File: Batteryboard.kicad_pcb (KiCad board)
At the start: 4 copper layers, 76.2 x 76.2 mm, 147 parts, among them IC1 FAN4010IL6X_F113, IC2 FAN4010IL6X_F113, IC3 FAN4010IL6X_F113, J1 Conn_01x02_Male, J2 Conn_01x03_Male, J3 Conn_01x05_Male, J4 Conn_01x02_Male, J5 SC_19-20, Q1 SI7617DN-T1-GE3, Q2 SI7617DN-T1-GE3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

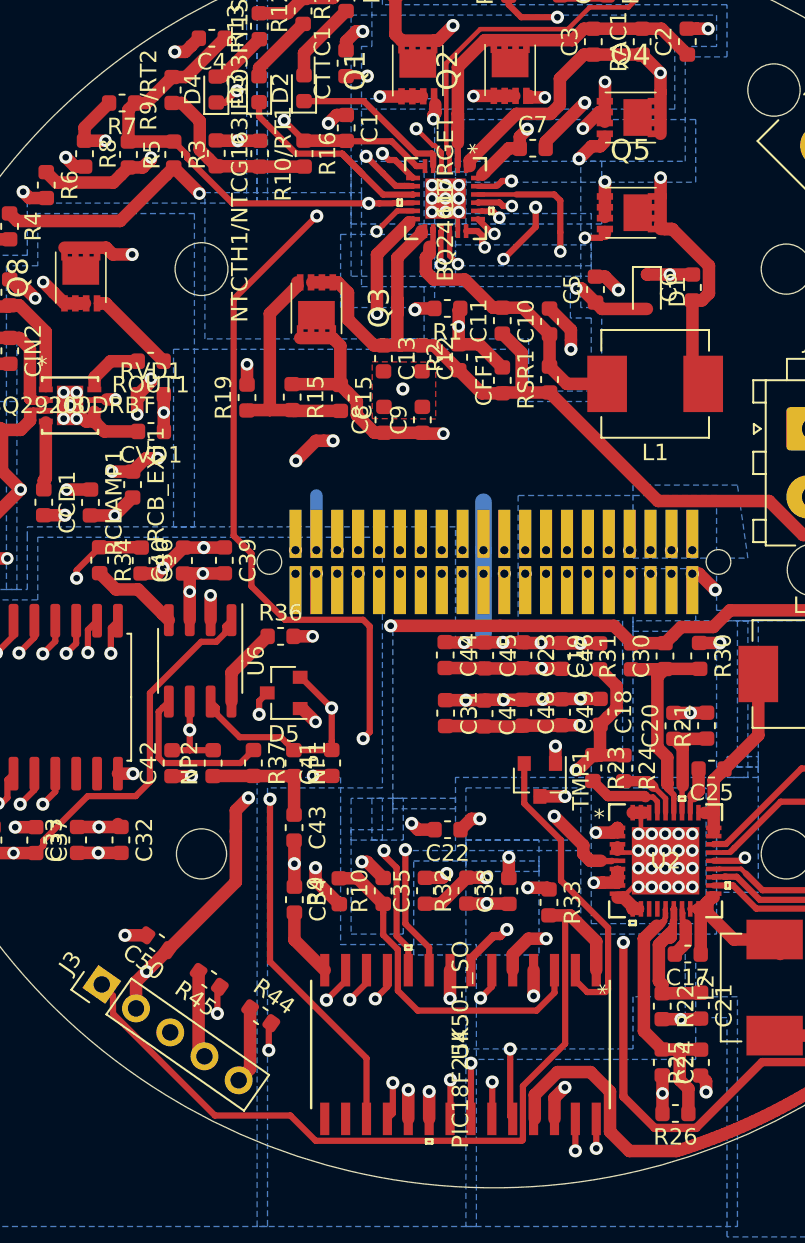
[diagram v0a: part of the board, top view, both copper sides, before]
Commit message: fixed some stuff, grounding and a few traces
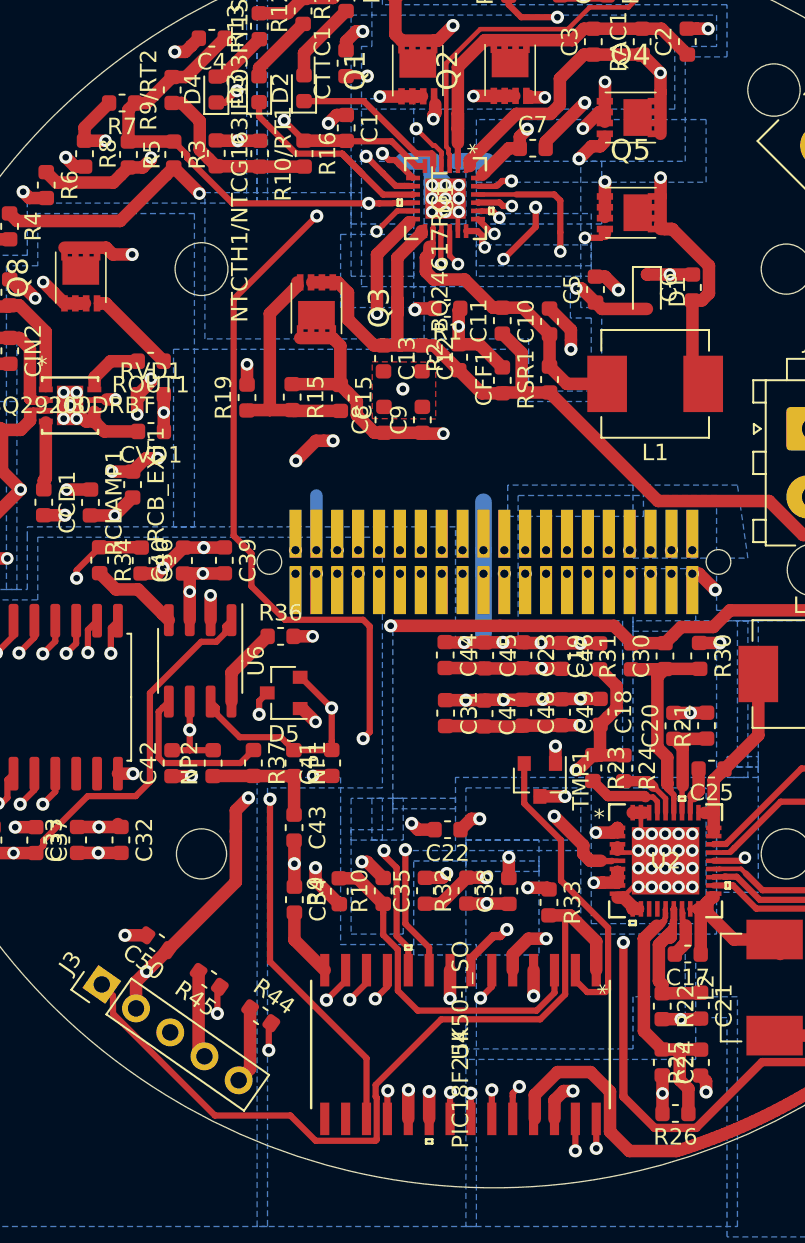
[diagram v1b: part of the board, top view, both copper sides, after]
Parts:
- added R_JUMP1: 0Ohm, Resistor_SMD:R_0603_1608Metric, B.Cu at (232.4, 38.7)
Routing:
- net PGND2: track 147.4 -> 156.1 mm
- net VBATCURRENT: track 44.3 -> 35.7 mm
- net 3V3: track 129.3 -> 134.2 mm
- net SI: track 58.8 -> 54.4 mm
- net SCK: track 61.6 -> 58.5 mm
- net MCLR: track 50.3 -> 48.7 mm
- net INT: track 61.2 -> 60.0 mm
- net PGC: track 26.1 -> 25.2 mm
- net CS: track 62.4 -> 61.6 mm

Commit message: fixed another little trace
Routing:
- net TS: track 85.7 -> 90.1 mm
- net MCLR: track 48.7 -> 49.3 mm

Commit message: big overhaul on board, did a bunch of stuff
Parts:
- C20, C21, C34, C35, C38, C50: value C -> .1uF
- C26, C27: value C -> 50nF
- J5: footprint MASA-LIB:bottom_Stack_Connector_2019_2020 -> MASA-LIB:Stack_Connector_2019_2020
- R10, R32, R9: value R_US -> 10kOhm
- R21, R22: value R_US -> 60.4kOhm
- R28: value R_US -> 30Ohm
- R33: value R_US -> 470Ohm
- R44, R45: value R_US -> 100Ohm
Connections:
- C1 pad 1: PGND2 -> VSS
- C10 pad 2: PGND2 -> VSS
- C2 pad 2: PGND2 -> VSS
- C20 pad 2: PGND2 -> VSS
- C21 pad 2: PGND2 -> VSS
- C26 pad 1: PGND2 -> VSS
- C27 pad 1: PGND2 -> VSS
- C28 pad 1: PGND2 -> VSS
- C29 pad 1: PGND2 -> VSS
- C32 pad 2: PGND2 -> VSS
- C33 pad 1: PGND2 -> VSS
- C34 pad 1: PGND2 -> VSS
- C35 pad 2: PGND2 -> VSS
- C36 pad 2: PGND2 -> VSS
- C37 pad 1: PGND2 -> VSS
- C38 pad 2: PGND2 -> VSS
- C39 pad 1: PGND2 -> VSS
- C4 pad 2: PGND2 -> VSS
- C40 pad 2: PGND2 -> VSS
- C41 pad 1: PGND2 -> VSS
- C42 pad 1: PGND2 -> VSS
- C43 pad 2: PGND2 -> VSS
- C50 pad 2: PGND2 -> VSS
- C7 pad 2: PGND2 -> VSS
- CTTC1 pad 2: PGND2 -> VSS
- D5 pad 1: PGND2 -> VSS
- IC1 pad 5: PGND2 -> VSS
- IC2 pad 5: PGND2 -> VSS
- IC3 pad 5: PGND2 -> VSS
- J3 pad 3: PGND2 -> VSS
- J5 pad 1: PGND2 -> VSS
- J5 pad 19: PGND2 -> VSS
- J5 pad 20: PGND2 -> VSS
- J5 pad 36: PGND2 -> VSS
- J5 pad 37: PGND2 -> VSS
- J5 pad 4: PGND2 -> VSS
- J5 pad 40: PGND2 -> VSS
- J5 pad 5: PGND2 -> VSS
- NTCTH1/NTCG163JF103FT1S1 pad 1: PGND2 -> VSS
- R1 pad 2: PGND2 -> VSS
- R10/RT1 pad 1: PGND2 -> VSS
- R21 pad 2: PGND2 -> VSS
- R22 pad 2: PGND2 -> VSS
- R25 pad 1: PGND2 -> VSS
- R28 pad 1: PGND2 -> VSS
- R30 pad 1: PGND2 -> VSS
- R36 pad 2: PGND2 -> VSS
- R38 pad 1: PGND2 -> VSS
- R4 pad 2: PGND2 -> VSS
- R41 pad 2: PGND2 -> VSS
- R42 pad 2: PGND2 -> VSS
- R6 pad 2: PGND2 -> VSS
- R8 pad 2: PGND2 -> VSS
- R_JUMP1 pad 1: PGND2 -> VSS
- TMP1 pad 3: PGND2 -> VSS
- U1 pad 25: PGND2 -> VSS
- U2 pad 23: PGND2 -> VSS
- U2 pad 3: PGND2 -> VSS
- U2 pad 4: PGND2 -> VSS
- U4 pad 19: PGND2 -> VSS
- U4 pad 8: PGND2 -> VSS
- U5 pad 18: PGND2 -> VSS
- U6 pad 2: PGND2 -> VSS
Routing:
- net VSS: track 0.00 -> 113.3 mm, vias 0 -> 47
- net PGND2: track 156.1 -> 57.7 mm, vias 94 -> 44
- net V7V: track 12.4 -> 14.3 mm
- net Net-(R19-Pad2): track 27.8 -> 28.9 mm
- net CAN_L: vias 3 -> 2
- net CAN_H: vias 2 -> 1
- net 5V0: vias 15 -> 11
- net 3V3: vias 8 -> 4
- added copper zone on B.Cu, net (none)
- added copper zone on B.Cu, net VSS

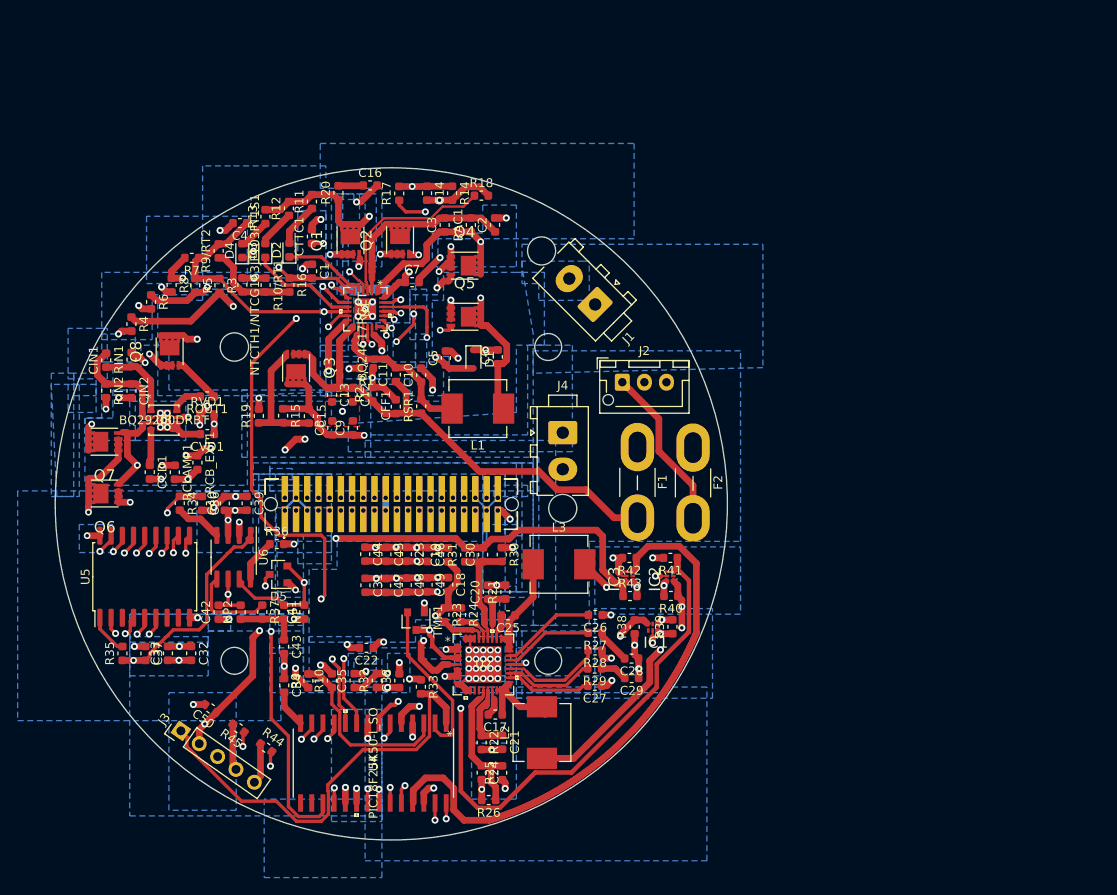
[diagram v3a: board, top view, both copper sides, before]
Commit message: basically an emergency backup, going to reroute my board
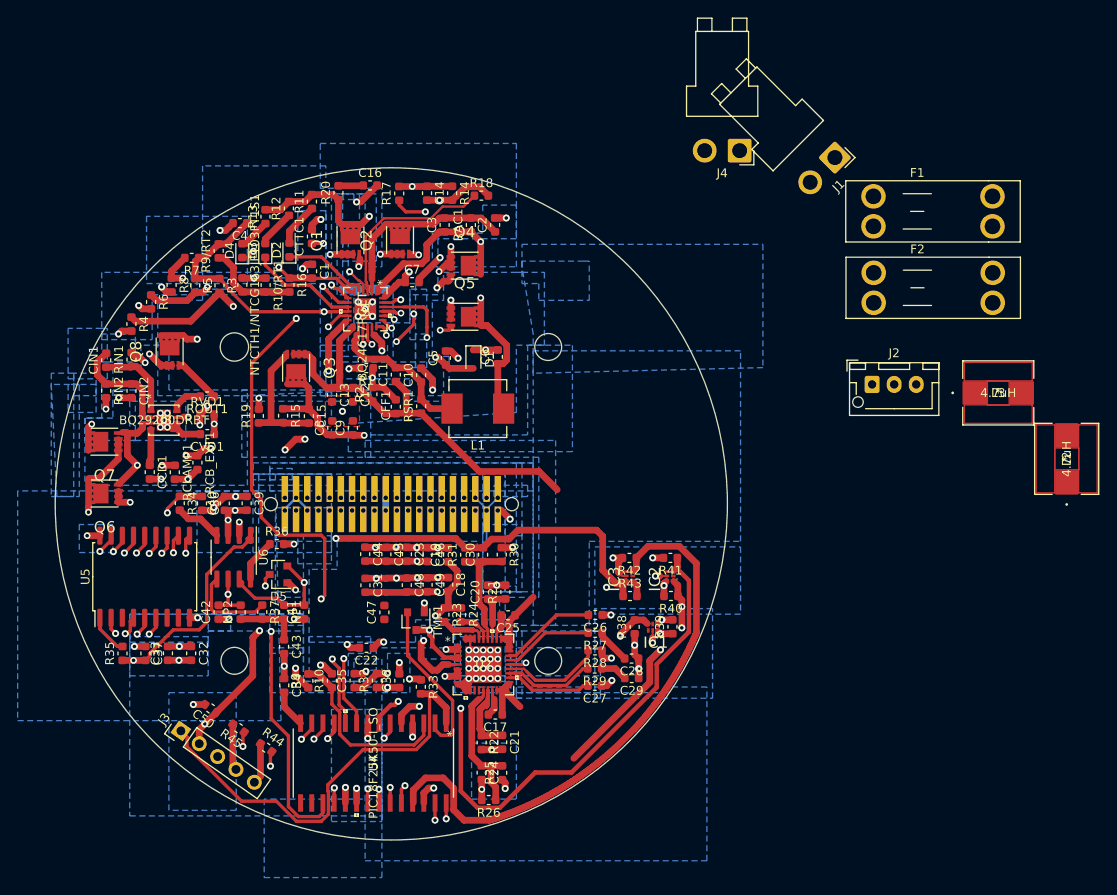
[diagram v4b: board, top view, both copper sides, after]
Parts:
- C20, C21: value .1uF -> 1nF
- C24, C30: value C -> 1nF
- C28, C29: value C -> .012uF
- C47: value 22uF -> 33uF
- F1, F2: footprint Fuse:Fuse_Blade_Mini_directSolder -> 3557-2:Fuseholder_Blade_Mini_Keystone_3557-2
- J1, J4: footprint Connector_TE-Connectivity:TE_MATE-N-LOK_1-770866-x_1x02_P4.14mm_Vertical -> Connector_JST:JST_VH_B2PS-VH_1x02_P3.96mm_Horizontal
- J5: footprint MASA-LIB:Stack_Connector_2019_2020 -> MASA-LIB:bottom_Stack_Connector_2019_2020
- L2, L3: footprint Inductor_SMD:L_Vishay_IHLP-2525 -> SRP7030-4R7M:SRP7030-4R7M
- R25: value R_US -> 5.36kOhm
- R26, R31: value R_US -> 40.2kOhm
- R27: value R_US -> 14kOhm
- R28: value 30Ohm -> 31Ohm
- R29: value R_US -> 9.31kOhm
- R30: value R_US -> 8.87kOhm
- R38, R41, R42: value R_US -> 5kOhm
- moved L2 67.1 mm to (311.9, 58.0)
- moved L3 53.4 mm to (304.2, 50.5)
- moved F1 39.0 mm to (290.0, 28.2), turned to 0 degrees
- moved J4 37.7 mm to (274.9, 23.0), turned to 180 degrees
- moved J1 31.9 mm to (285.6, 23.8)
- moved F2 28.5 mm to (290.0, 36.9), turned to 0 degrees
- moved J2 28.3 mm to (289.9, 49.5)
- moved C47 3.05 mm to (234.6, 75.4), turned to 90 degrees
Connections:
- C44 pad 2: Net-(C23-Pad2) -> Net-(C44-Pad2)
- C47 pad 1: PGND2 -> Net-(C47-Pad1)
- C47 pad 2: Net-(C31-Pad2) -> PGND2
- C8 pad 1: Q4D -> SRN
- C9 pad 1: Q4D -> SRN
- IC1 pad 1: Q4D -> SRN
- IC2 pad 1: Net-(C23-Pad2) -> Net-(C44-Pad2)
- IC3 pad 1: Net-(C31-Pad2) -> Net-(C47-Pad1)
- L2 pad 1: Net-(C23-Pad2) -> Net-(C44-Pad2)
- L3 pad 2: Net-(C31-Pad2) -> Net-(C47-Pad1)
- R39 pad 2: Q4D -> SRN
- R40 pad 1: Net-(C23-Pad2) -> Net-(C44-Pad2)
- R43 pad 2: Net-(C31-Pad2) -> Net-(C47-Pad1)
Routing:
- net Q6S: track 107.9 -> 71.1 mm
- net Net-(F2-Pad1): track 70.3 -> 50.5 mm
- net Net-(J2-Pad2): track 70.6 -> 51.8 mm
- net Net-(J1-Pad1): track 50.8 -> 35.5 mm
- net Net-(C31-Pad2): track 38.9 -> 27.7 mm, vias 3 -> 2
- net SRN: track 60.3 -> 49.9 mm
- net Net-(F1-Pad1): track 9.50 -> 0.00 mm
- net Net-(C23-Pad2): track 71.2 -> 67.1 mm
- net Net-(C47-Pad1): track 0.00 -> 3.73 mm
- net Net-(C25-Pad1): track 12.2 -> 8.51 mm
- net LX1: track 10.4 -> 7.41 mm
- net PGND2: track 57.7 -> 59.2 mm

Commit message: here u go matt, thanks for helping make this bomb
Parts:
- moved L2 65.5 mm to (254.1, 88.7)
- moved L3 52.6 mm to (255.3, 69.8), turned to 90 degrees
- moved RCB_EXT1 14.1 mm to (201.1, 51.5)
- moved R9 12.0 mm to (238.0, 83.7), turned to 270 degrees
- moved RVD1 8.15 mm to (208.2, 47.8), turned to 270 degrees
- moved R10 6.93 mm to (235.6, 83.7)
- moved R33 5.69 mm to (233.0, 83.6)
- moved C38 5.67 mm to (230.7, 83.7)
- moved R32 5.67 mm to (228.1, 83.6)
- moved C35 5.67 mm to (225.6, 83.6)
- moved CCD1 2.76 mm to (210.7, 59.0)
- moved RCLAMP1 2.39 mm to (208.5, 59.0), turned to 90 degrees
- moved Q8 2.09 mm to (212.3, 45.9)
- moved CVD1 1.90 mm to (214.5, 53.3), turned to 0 degrees
- moved C26 1.70 mm to (260.2, 75.7)
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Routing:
- net 3V3: track 134.2 -> 6.38 mm, vias 4 -> 0
- net Q4D: track 125.0 -> 5.58 mm, vias 3 -> 0
- net TS: track 90.1 -> 0.00 mm, vias 4 -> 0
- net VSS: track 113.3 -> 25.5 mm, vias 47 -> 7
- net Q6S: track 71.1 -> 1.14 mm, vias 4 -> 0
- net 5VCURRENT: track 67.2 -> 0.00 mm, vias 2 -> 0
- net 3V3CURRENT: track 65.2 -> 0.00 mm
- net Net-(C23-Pad2): track 67.1 -> 4.69 mm, vias 4 -> 0
- net CS: track 61.6 -> 0.00 mm, vias 2 -> 0
- net VBAT: track 69.1 -> 7.95 mm, vias 5 -> 0
- net INT: track 60.0 -> 0.00 mm, vias 2 -> 0
- net SO: track 59.9 -> 0.00 mm, vias 2 -> 0
- net SCK: track 58.5 -> 0.00 mm, vias 2 -> 0
- net SI: track 54.4 -> 0.00 mm, vias 2 -> 0
- net RESET: track 52.4 -> 0.00 mm, vias 2 -> 0
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- removed copper zone on B.Cu, net (none)

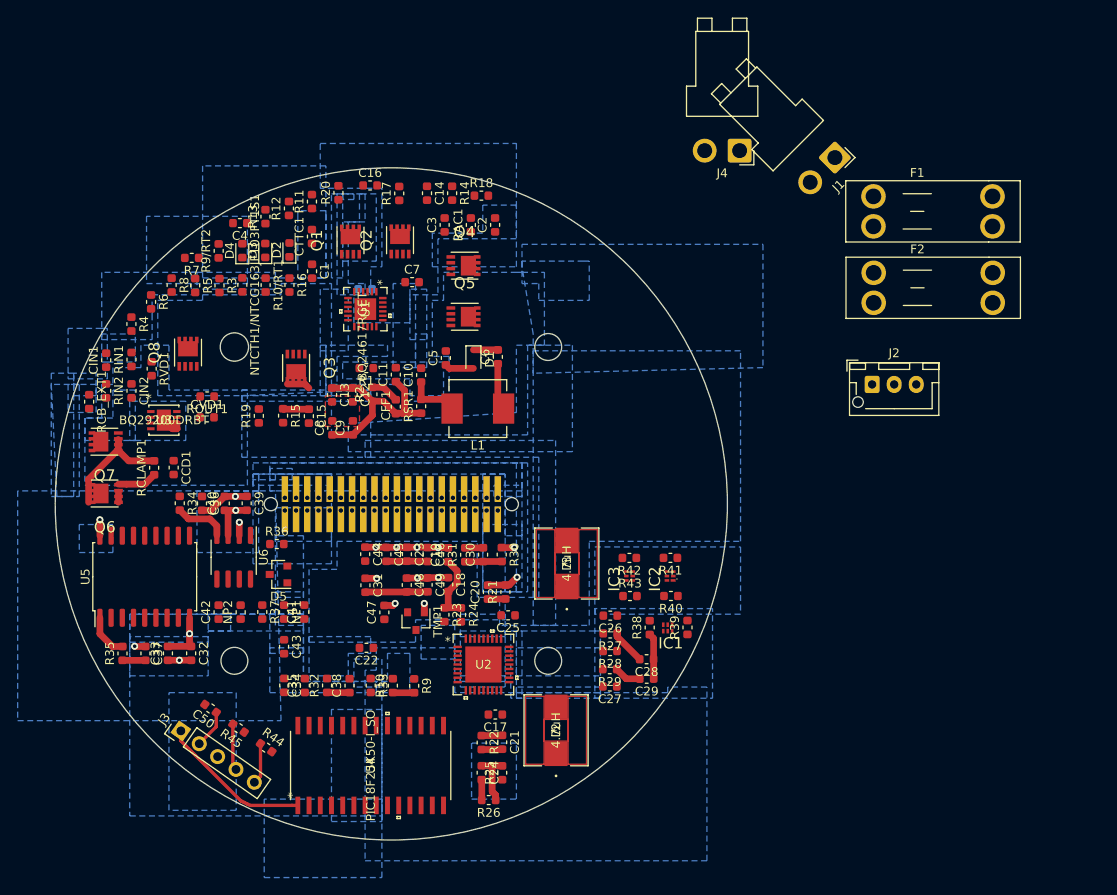
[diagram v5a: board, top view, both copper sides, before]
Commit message: schematic is final now, working on routing my board again
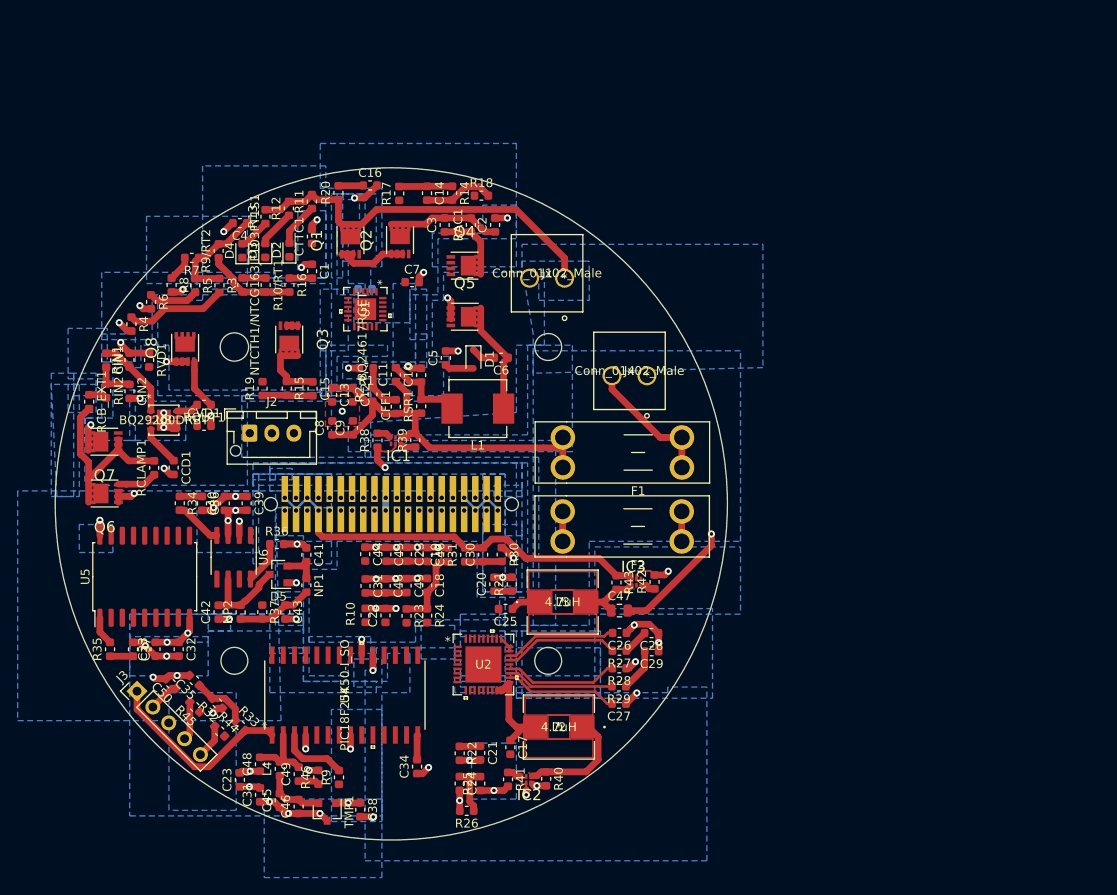
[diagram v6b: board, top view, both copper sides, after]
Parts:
- added C23: 1nF, Capacitor_SMD:C_0603_1608Metric, F.Cu at (218.2, 94.3)
- added C31: 100nF, Capacitor_SMD:C_0603_1608Metric, F.Cu at (220.5, 96.0)
- added C45: 1nF, Capacitor_SMD:C_0603_1608Metric, F.Cu at (222.7, 96.7)
- added C46: 100nF, Capacitor_SMD:C_0603_1608Metric, F.Cu at (224.9, 97.4)
- added C48: 100nF, Capacitor_SMD:C_0603_1608Metric, F.Cu at (220.5, 92.6)
- added C49: 2.2uF, Capacitor_SMD:C_0603_1608Metric, F.Cu at (224.9, 93.7)
- added L4: 2.2uH, Inductor_SMD:L_0603_1608Metric, F.Cu at (222.7, 93.1)
- added R46: 3.3Ohm, Resistor_SMD:R_0603_1608Metric, F.Cu at (227.1, 94.0)
- C47: footprint Capacitor_SMD:C_0603_1608Metric -> Capacitor_SMD:C_0805_2012Metric
- J1, J4: footprint Connector_JST:JST_VH_B2PS-VH_1x02_P3.96mm_Horizontal -> 1-1123723-2:1-1123723-2
- NP1, NP2: value 120 -> 60
- moved J2 70.7 mm to (219.3, 55.1)
- moved F1 37.6 mm to (268.3, 58.9), turned to 180 degrees
- moved R38 37.4 mm to (233.8, 55.9)
- moved IC1 37.4 mm to (235.9, 55.9)
- moved R39 37.4 mm to (238.1, 55.8)
- moved F2 37.4 mm to (268.3, 67.3), turned to 180 degrees
- moved J1 33.5 mm to (255.0, 37.5), turned to 180 degrees
- moved R41 31.1 mm to (248.6, 94.3), turned to 270 degrees
- moved IC2 28.3 mm to (250.7, 94.3), turned to 180 degrees
- moved J4 27.6 mm to (264.4, 48.6)
- moved C47 26.6 mm to (261.2, 75.2), turned to 0 degrees
- moved R40 25.1 mm to (252.9, 94.2), turned to 270 degrees
- moved TMP1 23.8 mm to (228.1, 98.0)
- moved C34 17.6 mm to (238.3, 92.8), turned to 90 degrees
- moved R33 15.5 mm to (218.3, 88.2), turned to 315 degrees
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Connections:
- TMP1 pad 2: TEMP_OUT -> Net-(C45-Pad2)
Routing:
- net VSS: track 25.5 -> 100.7 mm, vias 7 -> 42
- net Q6S: track 1.14 -> 47.3 mm, vias 0 -> 2
- net 3V3: track 6.38 -> 50.0 mm
- net Net-(J1-Pad1): track 0.00 -> 42.7 mm
- net PGND2: track 20.8 -> 53.8 mm, vias 8 -> 22
- net SRN: track 22.5 -> 48.5 mm
- net Net-(F1-Pad1): track 0.00 -> 15.1 mm
- net Net-(C14-Pad1): track 0.00 -> 14.5 mm
- net 5V0: track 17.1 -> 30.9 mm, vias 3 -> 11
- net Net-(R27-Pad2): track 0.00 -> 13.1 mm
- net Net-(C44-Pad2): track 0.00 -> 13.1 mm
- net Net-(R28-Pad2): track 0.00 -> 13.0 mm
- net Net-(C27-Pad2): track 0.00 -> 12.9 mm
- net Net-(C26-Pad2): track 0.00 -> 12.8 mm
- net Net-(C2-Pad1): track 0.00 -> 12.7 mm
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
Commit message: did my board again, heck yeah, actually quite happy with it this time
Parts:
- moved C44 34.2 mm to (260.7, 88.1), turned to 180 degrees
- moved C32 16.5 mm to (201.2, 66.4), turned to 90 degrees
- moved R35 14.2 mm to (209.0, 66.4), turned to 270 degrees
- moved C33 14.0 mm to (203.9, 66.4), turned to 270 degrees
- moved C37 13.1 mm to (206.4, 66.4), turned to 90 degrees
- moved RVD1 11.2 mm to (214.1, 56.1), turned to 180 degrees
- moved U5 3.07 mm to (208.0, 74.3), turned to 270 degrees
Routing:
- net TS: track 2.56 -> 88.7 mm, vias 0 -> 4
- net Net-(F2-Pad1): track 3.40 -> 73.1 mm, vias 0 -> 1
- net VBAT: track 10.8 -> 79.3 mm, vias 0 -> 5
- net 3V3: track 50.0 -> 106.5 mm, vias 0 -> 3
- net RX0BF: track 0.00 -> 46.5 mm, vias 0 -> 2
- net 3V3CURRENT: track 1.53 -> 47.7 mm, vias 0 -> 2
- net TX2RTS: track 0.00 -> 44.6 mm, vias 0 -> 2
- net VBATCURRENT: track 1.52 -> 46.0 mm, vias 0 -> 2
- net TX0RTS: track 0.00 -> 44.3 mm, vias 0 -> 2
- net TX1RTS: track 0.00 -> 43.6 mm, vias 0 -> 2
- net Net-(R18-Pad1): track 0.00 -> 41.2 mm, vias 0 -> 2
- net Q6S: track 47.3 -> 88.2 mm
- net RX1BF: track 0.00 -> 40.8 mm, vias 0 -> 2
- net Q4D: track 16.4 -> 49.9 mm, vias 0 -> 2
- net Net-(C7-Pad1): track 0.00 -> 32.2 mm, vias 0 -> 2
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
